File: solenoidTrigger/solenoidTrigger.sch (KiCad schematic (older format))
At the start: 48 parts, among them J8 CONN_02X03, P1 OSTTC03, P2 OSTTC02, P3 OSTTC08, P4 OSTTC03, P5 OSTTC03, Q1 NMOS_CDS16, Q2 NMOS_CDS16, Q3 NMOS_CDS16, Q4 NMOS_CDS16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

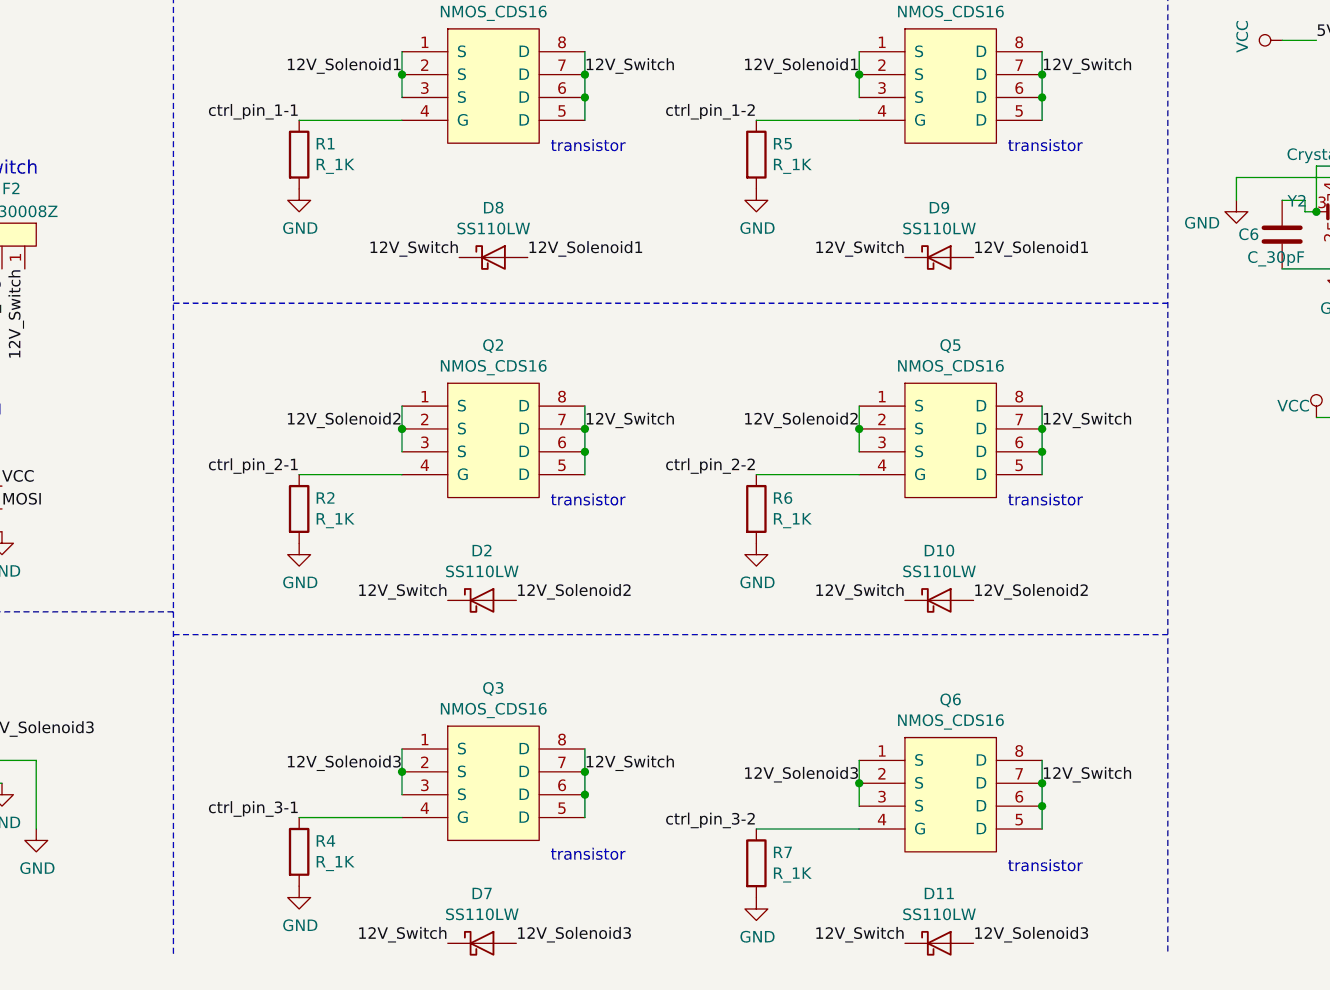
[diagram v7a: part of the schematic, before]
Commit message: deleted one flyback per solenoid
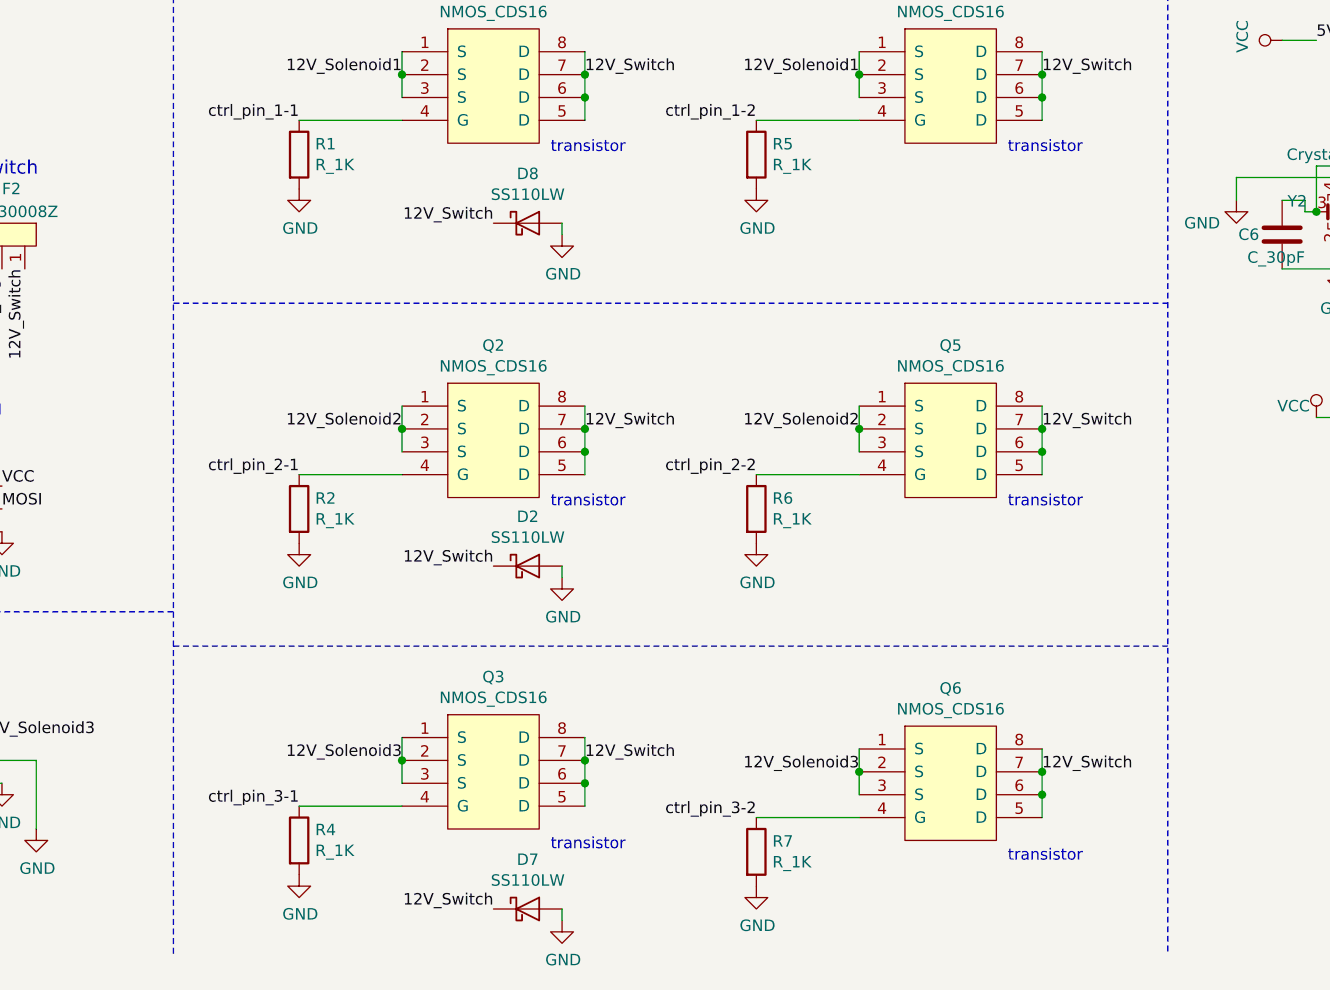
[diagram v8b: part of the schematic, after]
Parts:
- removed D10, D11, D9: SS110LW, footprints:D_SOD-123W_OEM, symbol Rocketry:SS110LW
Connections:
- net 12V_Solenoid1: no longer D8.2 (A)
- net 12V_Solenoid2: no longer D2.2 (A)
- net 12V_Solenoid3: no longer D7.2 (A)
- net GND: now also D2.2 (A), D7.2 (A), D8.2 (A)
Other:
- moved on the sheet: D2, D7, D8, Q3, Q6, R4, R7
